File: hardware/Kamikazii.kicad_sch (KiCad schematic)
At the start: 58 parts, among them M1 Motor, M2 Motor, SW1 210-4MS, T1 On/Off, T2 Remote Start, U1 DRV8871DDAR, U2 DRV8871DDAR, U3 BP, U4 L7805CV

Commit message: Finalize schematic
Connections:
- net GND: now also U1.9 (PAD), U2.9 (PAD)
- no-connect marks 15 -> 13
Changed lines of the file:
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@@
 		)
 	)
+	(text_box "Note: Create a GND pour directly under the chip and route external thermal vias to avoid via-in-pad."
+		(exclude_from_sim no)
+		(at 86.36 177.8 0)
+		(size 22.86 11.43)
+		(margins 0.9525 0.9525 0.9525 0.9525)
+		(stroke
+			(width 0)
+			(type solid)
+		)
+		(fill
+			(type none)
+		)
+		(effects
+			(font
+				(size 1.27 1.27)
+			)
+			(justify left top)
+		)
+	)
 	(junction
 		(at 158.75 74.93)
@@
 	)
 	(junction
+		(at 64.77 179.07)
+		(diameter 0)
+		(color 0 0 0 0)
+	)
+	(junction
 		(at 35.56 59.69)
 		(diameter 0)
@@
 	)
 	(junction
+		(at 143.51 179.07)
+		(diameter 0)
+		(color 0 0 0 0)
+	)
+	(junction
 		(at 166.37 128.27)
 		(diameter 0)
@@
 	)
 	(no_connect
-		(at 142.24 161.29)
-	)
-	(no_connect
 		(at 95.25 132.08)
 	)
@@
 	)
 	(no_connect
-		(at 63.5 161.29)
-	)
-	(no_connect
 		(at 95.25 78.74)
 	)
@@
 	(wire
 		(pts
+			(xy 143.51 179.07) (xy 152.4 179.07)
+		)
+		(stroke
+			(width 0)
+			(type default)
+		)
+	)
+	(wire
+		(pts
 			(xy 140.97 95.25) (xy 144.78 95.25)
 		)
@@
 	(wire
 		(pts
+			(xy 142.24 161.29) (xy 143.51 161.29)
+		)
+		(stroke
+			(width 0)
+			(type default)
+		)
+	)
+	(wire
+		(pts
 			(xy 27.94 81.28) (xy 35.56 81.28)
 		)
@@
 	(wire
 		(pts
+			(xy 64.77 179.07) (xy 73.66 179.07)
+		)
+		(stroke
+			(width 0)
+			(type default)
+		)
+	)
+	(wire
+		(pts
 			(xy 147.32 80.01) (xy 156.21 80.01)
 		)
@@
 	(wire
 		(pts
-			(xy 63.5 179.07) (xy 73.66 179.07)
+			(xy 63.5 179.07) (xy 64.77 179.07)
 		)
 		(stroke
@@
 	(wire
 		(pts
+			(xy 143.51 161.29) (xy 143.51 179.07)
+		)
+		(stroke
+			(width 0)
+			(type default)
+		)
+	)
+	(wire
+		(pts
 			(xy 31.75 73.66) (xy 35.56 73.66)
 		)
@@
 	(wire
 		(pts
-			(xy 142.24 179.07) (xy 152.4 179.07)
+			(xy 142.24 179.07) (xy 143.51 179.07)
 		)
 		(stroke
@@
 	(wire
 		(pts
+			(xy 63.5 161.29) (xy 64.77 161.29)
+		)
+		(stroke
+			(width 0)
+			(type default)
+		)
+	)
+	(wire
+		(pts
 			(xy 138.43 93.98) (xy 138.43 97.79)
 		)
@@
 	(wire
 		(pts
+			(xy 64.77 161.29) (xy 64.77 179.07)
+		)
+		(stroke
+			(width 0)
+			(type default)
+		)
+	)
+	(wire
+		(pts
 			(xy 138.43 100.33) (xy 140.97 100.33)
 		)
@@
 		(pin "VBAT"
 		)
-		(pin "BOOT"
+		(pin "SWCLK"
 		)
-		(pin "PB2"
+		(pin "SWO"
 		)
 		(instances

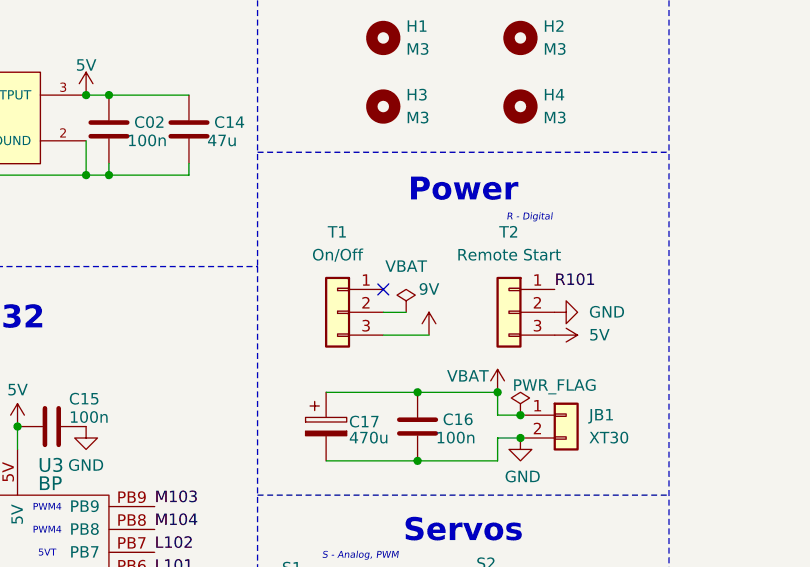
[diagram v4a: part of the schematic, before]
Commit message: Start routing and fix minor schematic mistakes
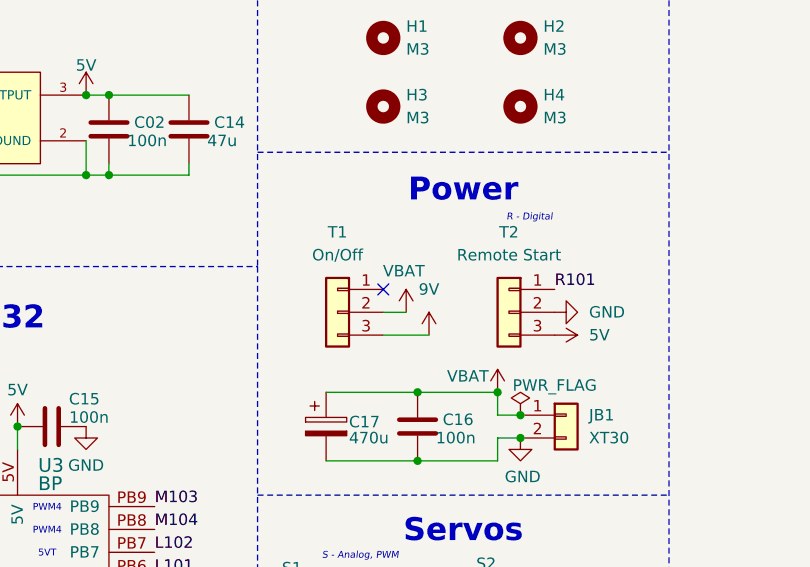
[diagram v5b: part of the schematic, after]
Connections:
- net VBAT: now also T1.2 (Pin_2)
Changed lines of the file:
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@@
-	)
-	(symbol
-		(lib_id "power:PWR_FLAG")
-		(at 146.05 63.5 0)
-		(unit 1)
-		(exclude_from_sim no)
-		(in_bom yes)
-		(on_board yes)
-		(dnp no)
-		(property "Reference" "#FLG01"
-			(at 146.05 61.595 0)
-			(effects
-				(font
-					(size 1.27 1.27)
-				)
-				(hide yes)
-			)
-		)
-		(property "Value" "VBAT"
-			(at 146.05 58.42 0)
-			(effects
-				(font
-					(size 1.27 1.27)
-				)
-			)
-		)
-		(property "Footprint" ""
-			(at 146.05 63.5 0)
-			(effects
-				(font
-					(size 1.27 1.27)
-				)
-				(hide yes)
-			)
-		)
-		(property "Datasheet" "~"
-			(at 146.05 63.5 0)
-			(effects
-				(font
-					(size 1.27 1.27)
-				)
-				(hide yes)
-			)
-		)
-		(property "Description" "Special symbol for telling ERC where power comes from"
-			(at 146.05 63.5 0)
-			(effects
-				(font
-					(size 1.27 1.27)
-				)
-				(hide yes)
-			)
-		)
-		(pin "1"
-		)
-		(instances
-			(project ""
-				(path "/7eee047e-cae0-4bb5-9533-e77158aae09e"
-					(reference "#FLG01")
-					(unit 1)
-				)
-			)
-		)
 	)
 	(symbol
@@
 					(unit 1)
 				)
+			)
+		)
+	)
+	(symbol
+		(lib_id "power:VCC")
+		(at 146.05 63.5 0)
+		(unit 1)
+		(exclude_from_sim no)
+		(in_bom yes)
+		(on_board yes)
+		(dnp no)
+		(property "Reference" "#PWR050"
+			(at 146.05 67.31 0)
+			(effects
+				(font
+					(size 1.27 1.27)
+				)
+				(hide yes)
+			)
+		)
+		(property "Value" "VBAT"
+			(at 145.796 58.928 0)
+			(effects
+				(font
+					(size 1.27 1.27)
+				)
+			)
+		)
+		(property "Footprint" ""
+			(at 146.05 63.5 0)
+			(effects
+				(font
+					(size 1.27 1.27)
+				)
+				(hide yes)
+			)
+		)
+		(property "Datasheet" ""
+			(at 146.05 63.5 0)
+			(effects
+				(font
+					(size 1.27 1.27)
+				)
+				(hide yes)
+			)
+		)
+		(property "Description" "Power symbol creates a global label with name \"VCC\""
+			(at 146.05 63.5 0)
+			(effects
+				(font
+					(size 1.27 1.27)
+				)
+				(hide yes)
+			)
+		)
+		(pin "1"
+		)
+		(instances
+			(project "Kamikazii"
+				(path "/7eee047e-cae0-4bb5-9533-e77158aae09e"
+					(reference "#PWR050")
+					(unit 1)
+				)

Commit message: Make minor adjustments to schematic and finish layout with no errors
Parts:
- added C20: 100n, Capacitor_SMD:C_0402_1005Metric, symbol Device:C
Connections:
- net 5V: now also C20.1
- net D101: now also U3.PB12; no longer U3.PB10
- net D102: now also U3.PB13; no longer U3.PB11
- net D103: now also U3.PB14; no longer U3.PB12
- net D104: now also U3.PB11; no longer U3.PB13
- net D105: now also U3.PB10; no longer U3.PB14
- net GND: now also C20.2
- net LED106: now also U3.PA1; no longer U3.PA0
- net LED107: now also U3.PA0; no longer U3.PA1
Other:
- moved on the sheet: T1, T2
